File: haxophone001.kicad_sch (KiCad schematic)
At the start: 79 parts, among them J1 Conn_02x02_Odd_Even, J10 Conn_02x02_Odd_Even, J3 Raspberry_Pi_2_3, J4 Conn_01x03_Male, J5 Line Out, J6 Conn_02x02_Odd_Even, J8 Conn_02x02_Odd_Even, U1 MPXV7007DP, U2 MCP3221, U4 MAX98357

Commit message: Revert back to previous audio connector
Revert back to audio connector C18594 from Boomele after receiving a
defect report for the part used in version 1.0.1.  This connector
was out of stock during Covid but now is well stocked.
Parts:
- J5: footprint haxo001:C381130 -> haxo001:C18594; LCSC C381130 -> C18594
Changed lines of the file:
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@@
       (effects (font (size 1.27 1.27)) (justify right))
     )
-    (property "Footprint" "haxo001:C381130" (id 2) (at 102.87 124.46 0)
+    (property "Footprint" "haxo001:C18594" (id 2) (at 102.87 124.46 0)
       (effects (font (size 1.27 1.27)) hide)
     )
@@
       (effects (font (size 1.27 1.27)) hide)
     )
-    (property "LCSC" "C381130" (id 4) (at 102.87 124.46 0)
+    (property "LCSC" "C18594" (id 4) (at 102.87 124.46 0)
       (effects (font (size 1.27 1.27)) hide)
     )
@@
     )
     (path "/00000000-0000-0000-0000-000060f0ae4a"
-      (reference "J5") (unit 1) (value "Line Out") (footprint "haxo001:C381130")
+      (reference "J5") (unit 1) (value "Line Out") (footprint "haxo001:C18594")
     )
     (path "/00000000-0000-0000-0000-0000609837ce"

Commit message: Add Alternate pressure sensor part
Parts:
- U1: Alternate (none) -> MPXV7007GC6U, MPXV7007GP
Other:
- company: Javier Cardona -> Cardona Bits
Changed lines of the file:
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@@
   (title_block
     (title "Haxophone")
-    (date "2021-08-27")
-    (rev "0.6")
-    (company "Javier Cardona")
+    (date "2023-09-14")
+    (rev "1.1")
+    (company "Cardona Bits")
   )
   (junction (at 166.37 44.45) (diameter 0) (color 0 0 0 0)
@@
       (effects (font (size 1.27 1.27)) hide)
     )
+    (property "Alternate" " MPXV7007GC6U, MPXV7007GP" (id 5) (at 62.23 53.34 0)
+      (effects (font (size 1.27 1.27)) hide)
+    )

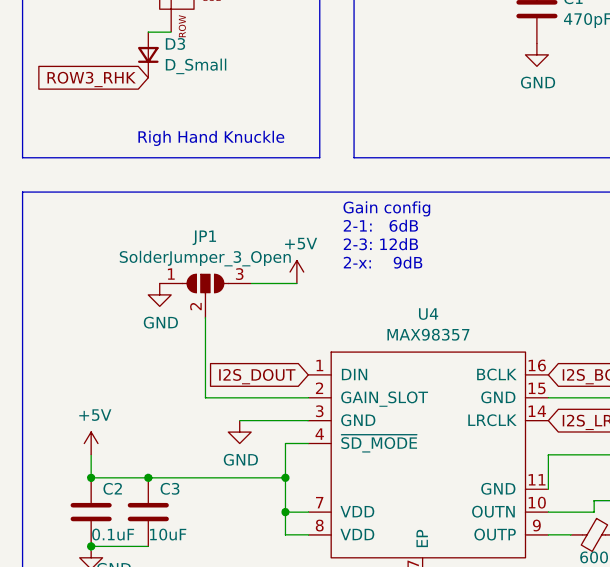
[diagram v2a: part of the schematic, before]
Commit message: Migrate to Kicad 7
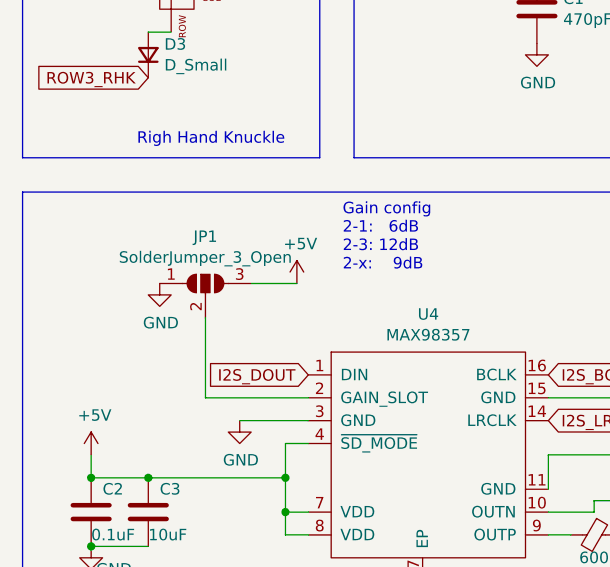
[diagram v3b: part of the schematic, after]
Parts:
- J4: symbol Connector:Conn_01x03_Male -> Connector:Conn_01x03_Pin; now in the parts list
- J5: symbol Connector:AudioJack3 -> Connector_Audio:AudioJack3

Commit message: Fix all DRC errors raised by new kicad version (7.0)
Remove OSHW footprint until we can resolve the DRC problems it
introduces.
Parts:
- MX4, MX7: footprint MX_Only:MXOnly-2U-NoLED -> MX_Only:MXOnly-1U-NoLED
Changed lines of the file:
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@@
       (effects (font (size 0.508 0.508)))
     )
-    (property "Footprint" "MX_Only:MXOnly-2U-NoLED" (at 167.005 95.885 0)
+    (property "Footprint" "MX_Only:MXOnly-1U-NoLED" (at 167.005 95.885 0)
       (effects (font (size 1.524 1.524)) hide)
     )
@@
       (effects (font (size 0.508 0.508)))
     )
-    (property "Footprint" "MX_Only:MXOnly-2U-NoLED" (at 167.005 145.415 0)
-      (effects (font (size 1.524 1.524)) hide)
-    )
+    (property "Footprint" "MX_Only:MXOnly-1U-NoLED" (at 167.005 145.415 0)
+      (effects (font (size 1.524 1.524)) hide)
+    )

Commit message: Swap cap that was out of stock
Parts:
- C3: LCSC C19702 -> C96446
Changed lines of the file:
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@@
       (effects (font (size 1.27 1.27)) hide)
     )
-    (property "LCSC" "C19702" (at 27.94 123.19 0)
+    (property "LCSC" "C96446" (at 27.94 123.19 0)
       (effects (font (size 1.27 1.27)) hide)
     )

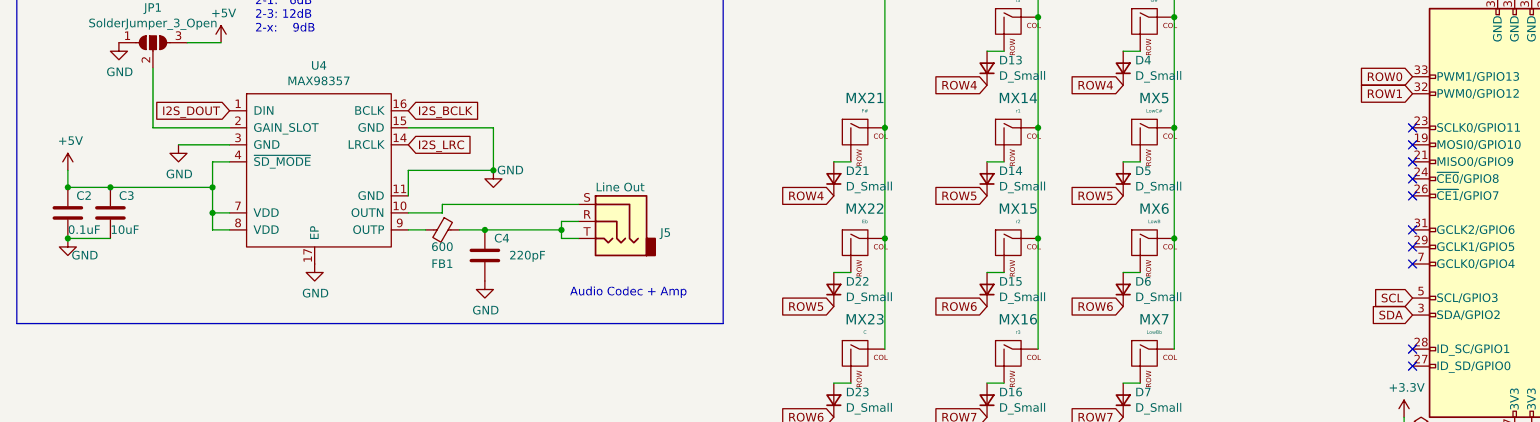
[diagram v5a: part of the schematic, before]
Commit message: Connect MAX98357a SD_MODE pin to GPIO4
SD_MODE pin can be used to eliminate start-up pop
GPIO4 seems to be the default pin according to
https://github.com/raspberrypi/linux/blob/rpi-6.1.y/arch/arm/boot/dts/overlays/max98357a-overlay.dts

See cardonabits/haxo-rs#17
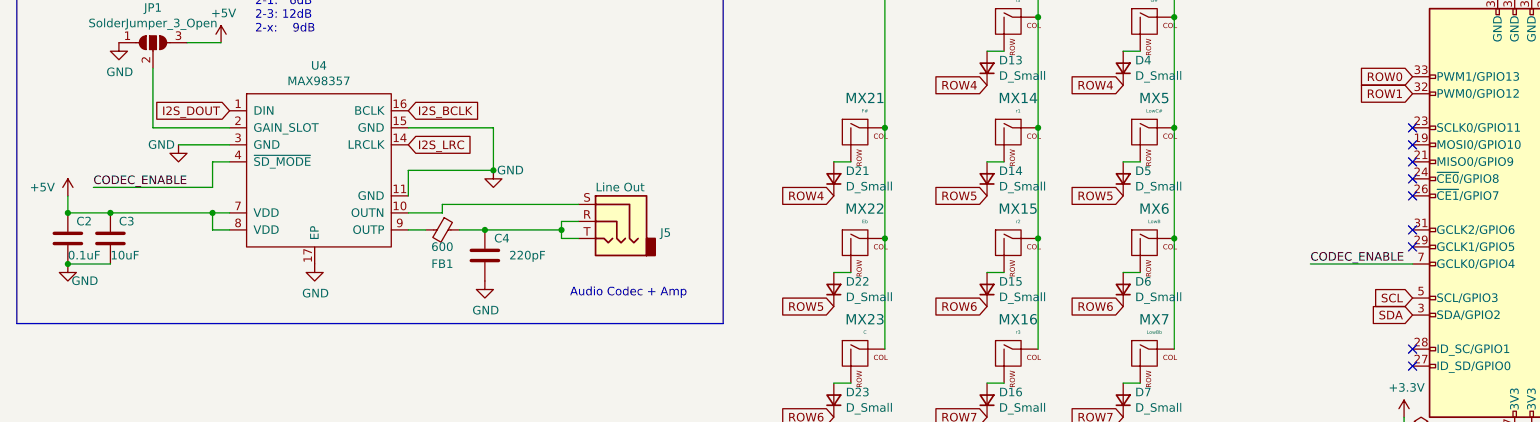
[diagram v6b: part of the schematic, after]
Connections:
- net +5V: no longer U4.4 (~{SD_MODE})
- net CODEC_ENABLE: now reaches J3.7 (GCLK0/GPIO4)
- net CODEC_ENABLE: now also U4.4 (~{SD_MODE})
- no-connect marks 12 -> 11
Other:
- moved on the sheet: C2, C3
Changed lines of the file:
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@@
   (junction (at 166.37 44.45) (diameter 0) (color 0 0 0 0)
   )
-  (junction (at 21.59 127) (diameter 0) (color 0 0 0 0)
+  (junction (at 21.59 130.81) (diameter 0) (color 0 0 0 0)
   )
   (junction (at 265.43 34.29) (diameter 0) (color 0 0 0 0)
   )
-  (junction (at 27.94 119.38) (diameter 0) (color 0 0 0 0)
+  (junction (at 27.94 123.19) (diameter 0) (color 0 0 0 0)
   )
   (junction (at 186.69 127) (diameter 0) (color 0 0 0 0)
@@
   (junction (at 104.14 64.77) (diameter 0) (color 0 0 0 0)
   )
-  (junction (at 21.59 119.38) (diameter 0) (color 0 0 0 0)
+  (junction (at 21.59 123.19) (diameter 0) (color 0 0 0 0)
   )
   (junction (at 186.69 110.49) (diameter 0) (color 0 0 0 0)
@@
   (junction (at 96.52 62.23) (diameter 0) (color 0 0 0 0)
   )
-  (junction (at 43.18 123.19) (diameter 0) (color 0 0 0 0)
-  )
   (junction (at 166.37 27.94) (diameter 0) (color 0 0 0 0)
   )
@@
   (junction (at 166.37 127) (diameter 0) (color 0 0 0 0)
   )
-  (junction (at 43.18 119.38) (diameter 0) (color 0 0 0 0)
+  (junction (at 43.18 123.19) (diameter 0) (color 0 0 0 0)
   )
   (junction (at 240.03 90.17) (diameter 0) (color 0 0 0 0)
@@
   (junction (at 166.37 93.98) (diameter 0) (color 0 0 0 0)
   )
-  (no_connect (at 222.25 130.81))
   (no_connect (at 222.25 143.51))
   (no_connect (at 222.25 113.03))
@@
   (no_connect (at 222.25 125.73))
   (no_connect (at 222.25 110.49))
-  (wire (pts (xy 43.18 123.19) (xy 43.18 125.73))
-    (stroke (width 0) (type default))
-  )
   (wire (pts (xy 74.93 58.42) (xy 74.93 60.96))
     (stroke (width 0) (type default))
@@
     (stroke (width 0) (type default))
   )
-  (wire (pts (xy 43.18 115.57) (xy 43.18 119.38))
-    (stroke (width 0) (type default))
-  )
   (wire (pts (xy 77.47 123.19) (xy 77.47 121.92))
     (stroke (width 0) (type default))
@@
     (stroke (width 0) (type default))
   )
-  (wire (pts (xy 45.72 123.19) (xy 43.18 123.19))
+  (wire (pts (xy 43.18 125.73) (xy 43.18 123.19))
     (stroke (width 0) (type default))
   )
@@
     (stroke (width 0) (type default))
   )
+  (wire (pts (xy 45.72 125.73) (xy 43.18 125.73))
+    (stroke (width 0) (type default))
+  )
   (polyline (pts (xy 172.72 166.37) (xy 172.72 195.58))
     (stroke (width 0) (type default))
@@
     (stroke (width 0) (type default))
   )
-  (wire (pts (xy 45.72 125.73) (xy 43.18 125.73))
-    (stroke (width 0) (type default))
-  )
   (wire (pts (xy 245.11 90.17) (xy 247.65 90.17))
     (stroke (width 0) (type default))
@@
     (stroke (width 0) (type default))
   )
-  (wire (pts (xy 158.75 82.55) (xy 161.29 82.55))
+  (wire (pts (xy 25.4 119.38) (xy 43.18 119.38))
     (stroke (width 0) (type default))
   )
-  (wire (pts (xy 43.18 123.19) (xy 43.18 119.38))
+  (wire (pts (xy 158.75 82.55) (xy 161.29 82.55))
     (stroke (width 0) (type default))
   )
@@
     (stroke (width 0) (type default))
   )
-  (wire (pts (xy 21.59 119.38) (xy 27.94 119.38))
+  (wire (pts (xy 21.59 123.19) (xy 27.94 123.19))
     (stroke (width 0) (type default))
   )
@@
     (stroke (width 0) (type default))
   )
-  (wire (pts (xy 21.59 127) (xy 27.94 127))
+  (wire (pts (xy 21.59 130.81) (xy 27.94 130.81))
+    (stroke (width 0) (type default))
+  )
+  (wire (pts (xy 207.01 130.81) (xy 222.25 130.81))
     (stroke (width 0) (type default))
   )
@@
     (stroke (width 0) (type default))
   )
-  (wire (pts (xy 21.59 119.38) (xy 21.59 116.84))
+  (wire (pts (xy 21.59 123.19) (xy 21.59 120.65))
     (stroke (width 0) (type default))
   )
@@
     (stroke (width 0) (type default))
   )
+  (wire (pts (xy 43.18 123.19) (xy 45.72 123.19))
+    (stroke (width 0) (type default))
+  )
   (wire (pts (xy 95.25 125.73) (xy 95.25 127))
     (stroke (width 0) (type default))
@@
     (stroke (width 0) (type default))
   )
-  (wire (pts (xy 27.94 119.38) (xy 43.18 119.38))
+  (wire (pts (xy 27.94 123.19) (xy 43.18 123.19))
     (stroke (width 0) (type default))
   )
@@
     (stroke (width 0) (type default))
   )
+  (wire (pts (xy 43.18 119.38) (xy 43.18 115.57))
+    (stroke (width 0) (type default))
+  )
   (text "4-pin right angle connectors used \nto join main PCB with both upper \nright and upper left PCBs."
     (at 77.47 36.83 0)
@@
     (effects (font (size 1.27 1.27)) (justify left bottom))
   )
+  (label "CODEC_ENABLE" (at 207.01 130.81 0) (fields_autoplaced)
+    (effects (font (size 1.27 1.27)) (justify left bottom))
+  )
+  (label "CODEC_ENABLE" (at 25.4 119.38 0) (fields_autoplaced)
+    (effects (font (size 1.27 1.27)) (justify left bottom))
+  )
   (global_label "ROW5" (shape input) (at 158.75 120.65 180) (fields_autoplaced)
     (effects (font (size 1.27 1.27)) (justify right))
@@
     )
   )
-  (symbol (lib_id "Device:C") (at 27.94 123.19 0) (unit 1)
+  (symbol (lib_id "Device:C") (at 27.94 127 0) (unit 1)
     (in_bom yes) (on_board yes) (dnp no)
-    (property "Reference" "C3" (at 29.21 120.65 0)
+    (property "Reference" "C3" (at 29.21 124.46 0)
       (effects (font (size 1.27 1.27)) (justify left))
     )
-    (property "Value" "10uF" (at 27.94 125.73 0)
+    (property "Value" "10uF" (at 27.94 129.54 0)
       (effects (font (size 1.27 1.27)) (justify left))
     )
-    (property "Footprint" "Capacitor_SMD:C_0603_1608Metric" (at 28.9052 127 0)
+    (property "Footprint" "Capacitor_SMD:C_0603_1608Metric" (at 28.9052 130.81 0)
       (effects (font (size 1.27 1.27)) hide)
     )
-    (property "Datasheet" "~" (at 27.94 123.19 0)
+    (property "Datasheet" "~" (at 27.94 127 0)
       (effects (font (size 1.27 1.27)) hide)
     )
-    (property "LCSC" "C96446" (at 27.94 123.19 0)
+    (property "LCSC" "C96446" (at 27.94 127 0)
       (effects (font (size 1.27 1.27)) hide)
     )
@@
     )
   )
-  (symbol (lib_id "Device:C") (at 21.59 123.19 0) (unit 1)
+  (symbol (lib_id "Device:C") (at 21.59 127 0) (unit 1)
     (in_bom yes) (on_board yes) (dnp no)
-    (property "Reference" "C2" (at 22.86 120.65 0)
+    (property "Reference" "C2" (at 22.86 124.46 0)
       (effects (font (size 1.27 1.27)) (justify left))
     )
-    (property "Value" "0.1uF" (at 21.59 125.73 0)
+    (property "Value" "0.1uF" (at 21.59 129.54 0)
       (effects (font (size 1.27 1.27)) (justify left))
     )
-    (property "Footprint" "Capacitor_SMD:C_0603_1608Metric" (at 22.5552 127 0)
+    (property "Footprint" "Capacitor_SMD:C_0603_1608Metric" (at 22.5552 130.81 0)
       (effects (font (size 1.27 1.27)) hide)
     )
-    (property "Datasheet" "~" (at 21.59 123.19 0)
+    (property "Datasheet" "~" (at 21.59 127 0)
       (effects (font (size 1.27 1.27)) hide)
     )
-    (property "LCSC" "C28323" (at 21.59 123.19 0)
+    (property "LCSC" "C28323" (at 21.59 127 0)
       (effects (font (size 1.27 1.27)) hide)
     )
@@
     )
   )
-  (symbol (lib_id "power:GND") (at 21.59 127 0) (unit 1)
+  (symbol (lib_id "power:GND") (at 21.59 130.81 0) (unit 1)
     (in_bom yes) (on_board yes) (dnp no)
-    (property "Reference" "#PWR010" (at 21.59 133.35 0)
+    (property "Reference" "#PWR010" (at 21.59 137.16 0)
       (effects (font (size 1.27 1.27)) hide)
     )
-    (property "Value" "GND" (at 24.13 129.54 0)
+    (property "Value" "GND" (at 24.13 133.35 0)
       (effects (font (size 1.27 1.27)))
     )
-    (property "Footprint" "" (at 21.59 127 0)
+    (property "Footprint" "" (at 21.59 130.81 0)
       (effects (font (size 1.27 1.27)) hide)
     )
-    (property "Datasheet" "" (at 21.59 127 0)
+    (property "Datasheet" "" (at 21.59 130.81 0)
       (effects (font (size 1.27 1.27)) hide)
     )
@@
     )
   )
-  (symbol (lib_id "power:+5V") (at 21.59 116.84 0) (unit 1)
+  (symbol (lib_id "power:+5V") (at 21.59 120.65 0) (unit 1)
     (in_bom yes) (on_board yes) (dnp no)
-    (property "Reference" "#PWR09" (at 21.59 120.65 0)
+    (property "Reference" "#PWR09" (at 21.59 124.46 0)
       (effects (font (size 1.27 1.27)) hide)
     )
-    (property "Value" "+5V" (at 21.971 112.4458 0)
+    (property "Value" "+5V" (at 17.78 119.38 0)
       (effects (font (size 1.27 1.27)))
     )
-    (property "Footprint" "" (at 21.59 116.84 0)
+    (property "Footprint" "" (at 21.59 120.65 0)
       (effects (font (size 1.27 1.27)) hide)
     )
-    (property "Datasheet" "" (at 21.59 116.84 0)
+    (property "Datasheet" "" (at 21.59 120.65 0)
       (effects (font (size 1.27 1.27)) hide)
     )
@@
       (effects (font (size 1.27 1.27)) hide)
     )
-    (property "Value" "GND" (at 38.227 117.4242 0)
+    (property "Value" "GND" (at 35.56 113.03 0)
       (effects (font (size 1.27 1.27)))
     )
